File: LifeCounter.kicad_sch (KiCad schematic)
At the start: 29 parts, among them IC1 STM32H562RGT6, IC2 AP3012KTR-E1, IC3 MCP73831T-2ATI_OT, J1 54104-4531, J2 USB_C_Receptacle_USB2.0_14P

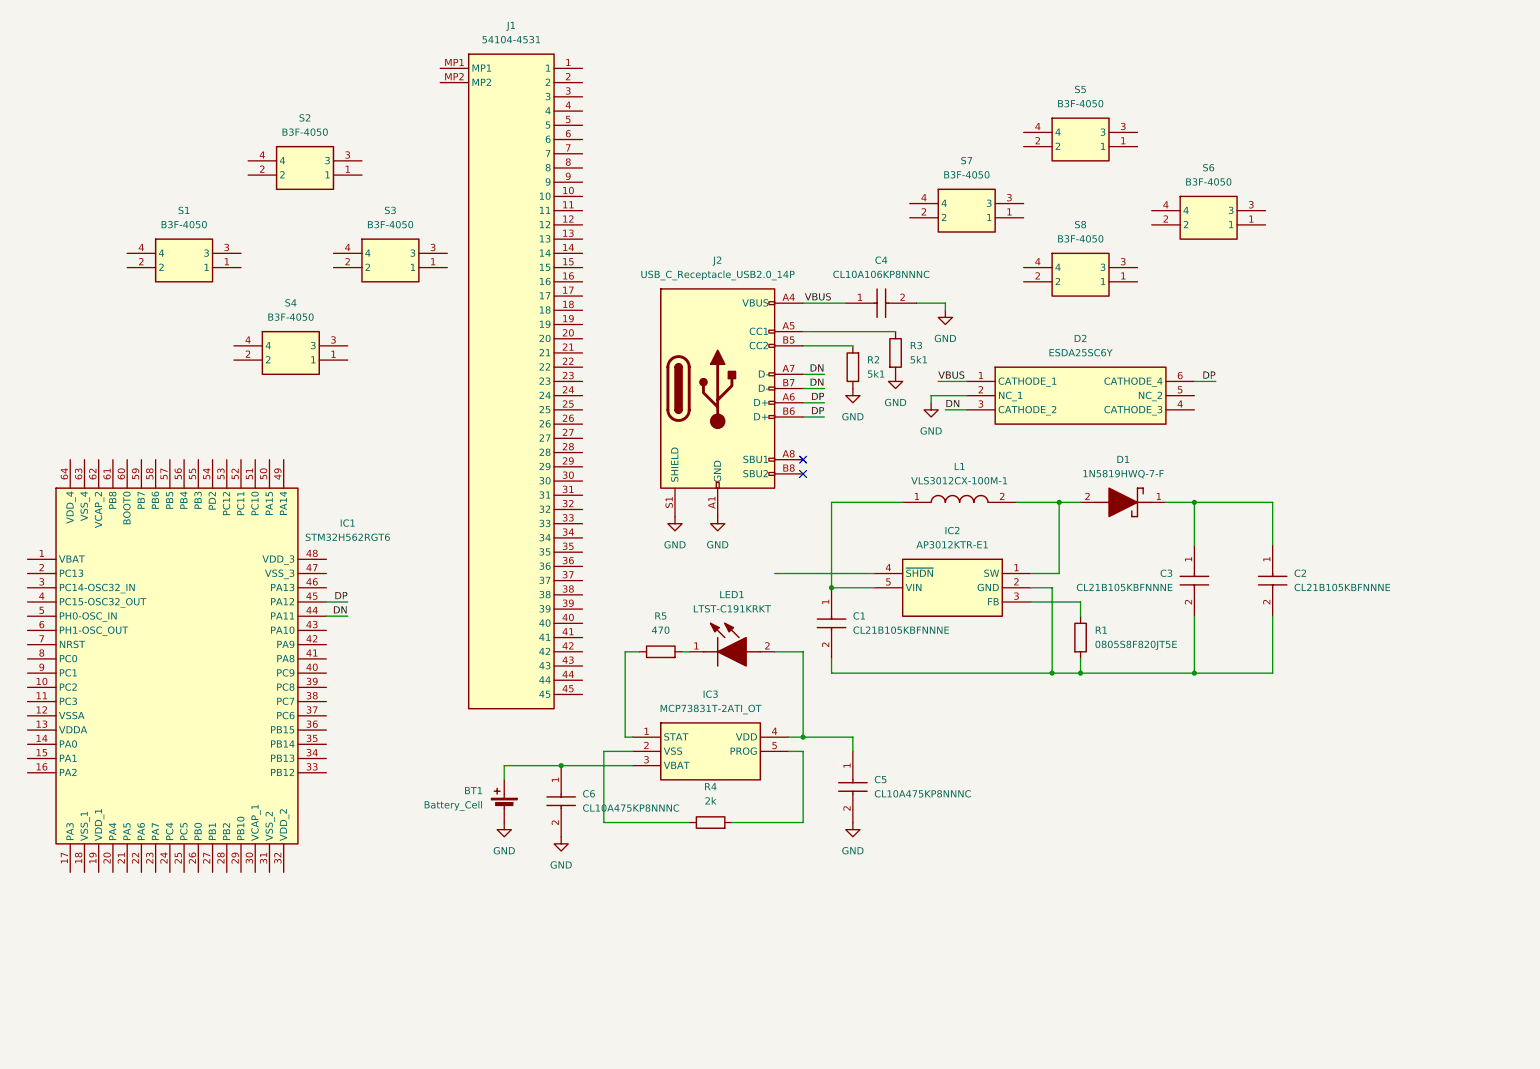
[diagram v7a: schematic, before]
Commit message: added LDO for 3v3 power delivery and a 100nF capacitor
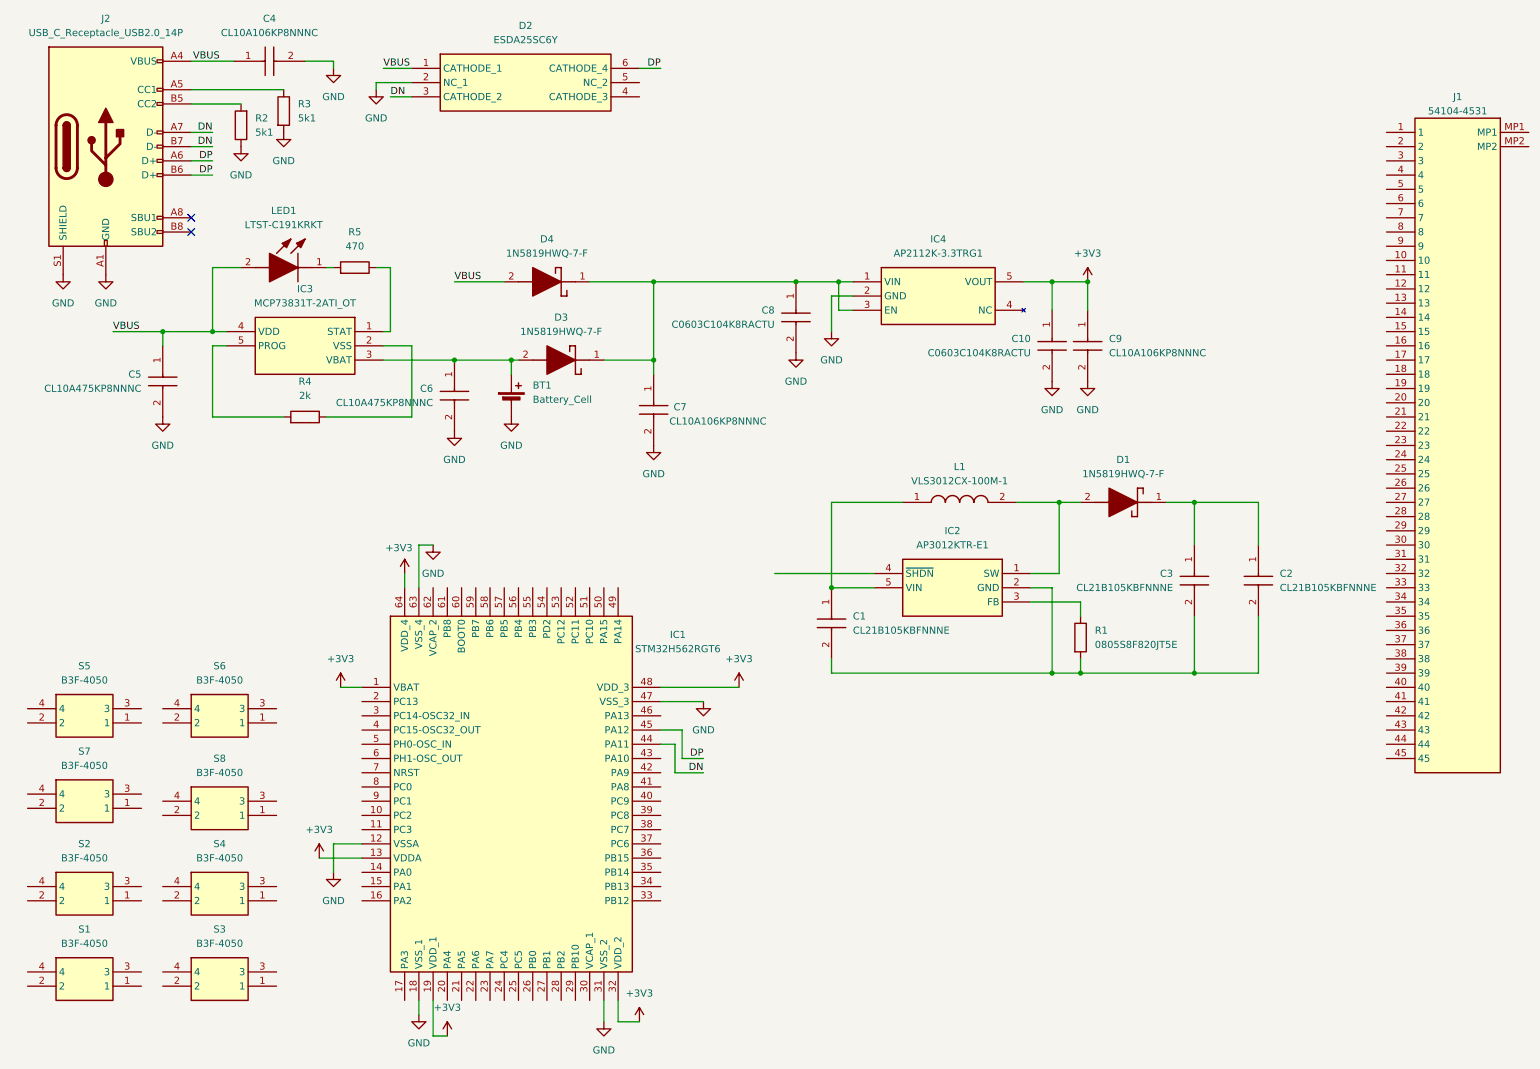
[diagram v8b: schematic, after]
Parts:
- added C10, C8: C0603C104K8RACTU, LifeCounter-Footprints:Kemet_C0603, symbol LifeCounter-Symbols:C0603C104K8RACTU
- added C7, C9: CL10A106KP8NNNC, LifeCounter-Footprints:Samsung_CAPC1608X90M, symbol LifeCounter-Symbols:CL10A106KP8NNNC
- added D3, D4: 1N5819HWQ-7-F, LifeCounter-Footprints:Diodes-Inc_SOD3716X145M, symbol LifeCounter-Symbols:1N5819HWQ-7-F
- added IC4: AP2112K-3.3TRG1, LifeCounter-Footprints:Diodes_Inc-SOT95P285X140-5M, symbol LifeCounter-Symbols:AP2112K-3.3TRG1
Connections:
- net GND: now also IC1.12 (VSSA), IC1.18 (VSS_1), IC1.31 (VSS_2), IC1.47 (VSS_3), IC1.63 (VSS_4), C10.2, C7.2, C8.2, C9.2, IC4.2 (GND)
- net VBUS: now also C5.1, IC3.4 (VDD), LED1.2 (A), D4.2 (A)
- net at BT1.1 (+), C6.1, IC3.3 (VBAT): now also D3.2 (A)
- net +3V3: now reaches IC1.1 (VBAT)
- net +3V3: now also IC1.13 (VDDA), IC1.19 (VDD_1), IC1.32 (VDD_2), IC1.48 (VDD_3), IC1.64 (VDD_4), C10.1, C9.1, IC4.5 (VOUT)
- new net: C7.1, C8.1, D3.1 (K), D4.1 (K), IC4.1 (VIN), IC4.3 (EN)
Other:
- moved on the sheet: BT1, C2, C4, C5, C6, D2, IC1, IC3, J1, J2, LED1, R2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
